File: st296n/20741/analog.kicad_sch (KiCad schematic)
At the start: 189 parts, among them J3 POWER, J4 SPINDLE, J5 STEPPER, J6 HEADS, Q1 ?, Q10 ?, Q11 ?, Q12 ?, Q15 "1A", Q2 2SD1760, Q3 IRFD110, Q4 IRFD110, Q5 IRFD110, Q8 ?, Q9 ?, U27 74LS00, U3 74LS14, U8 11747-501

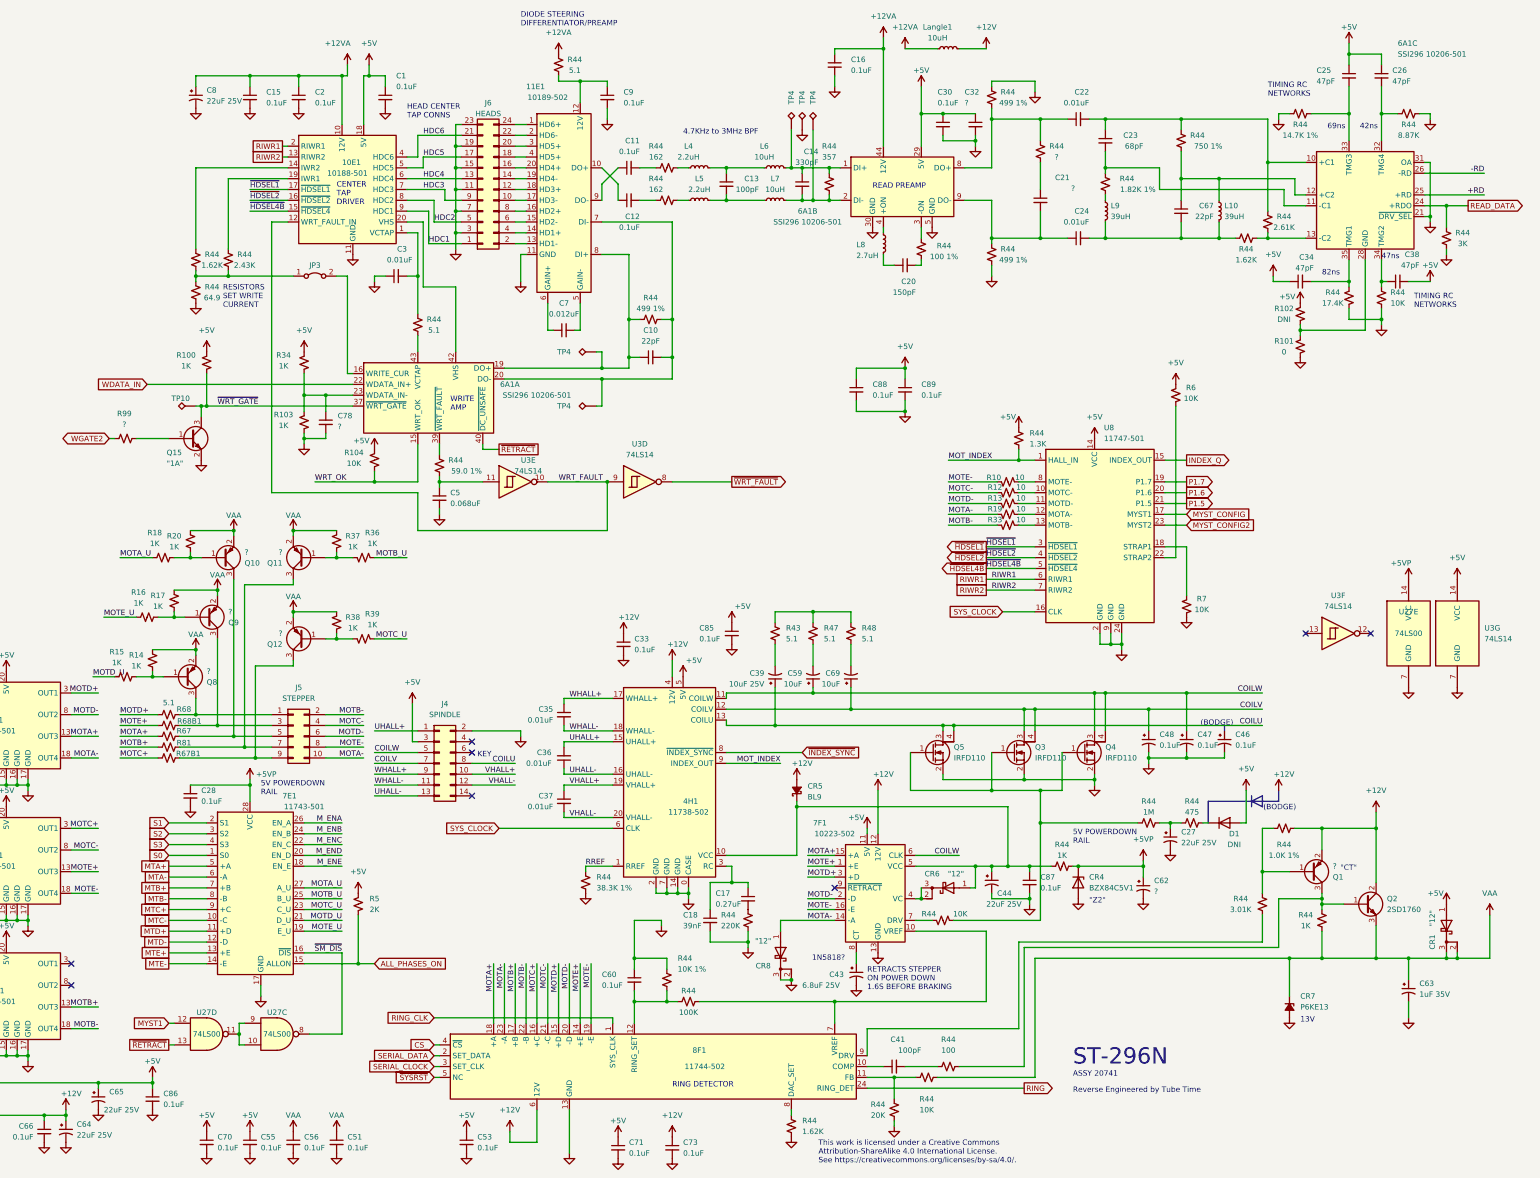
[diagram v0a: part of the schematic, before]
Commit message: st296n fix passives
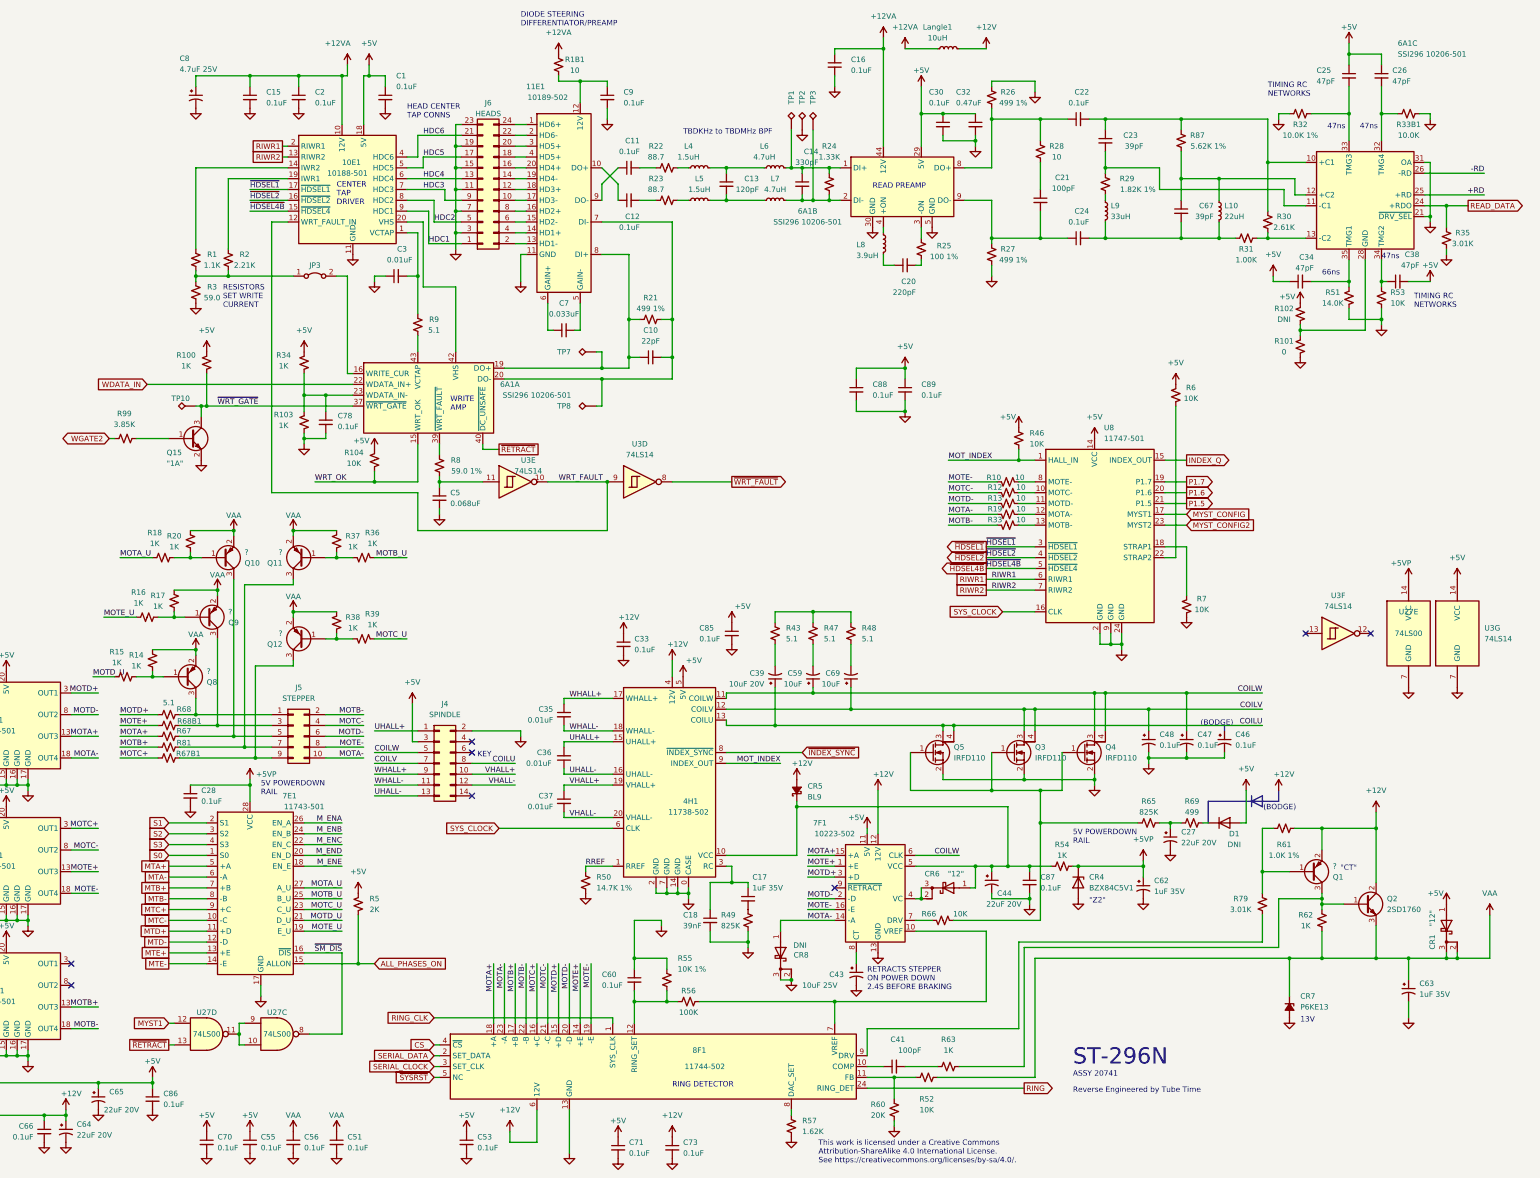
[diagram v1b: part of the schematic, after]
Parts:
- C13: value 100pF -> 120pF
- C17: value 0.27uF -> 1uF 35V
- C20: value 150pF -> 220pF
- C21: value ? -> 100pF
- C22, C24: value 0.01uF -> 0.1uF
- C23: value 68pF -> 39pF
- C27, C44, C64, C65: value 22uF 25V -> 22uF 20V
- C32: value ? -> 0.47uF
- C39: value 10uF 25V -> 10uF 20V
- C43: value 6.8uF 25V -> 10uF 25V
- C62: value ? -> 1uF 35V
- C67: value 22pF -> 39pF
- C7: value 0.012uF -> 0.033uF
- C78: value ? -> 0.1uF
- C8: value 22uF 25V -> 4.7uF 25V
- CR8: value "12" -> DNI
- L10: value 39uH -> 22uH
- L4, L5: value 2.2uH -> 1.5uH
- L6, L7: value 10uH -> 4.7uH
- L8: value 2.7uH -> 3.9uH
- L9: value 39uH -> 33uH
- R1: renamed from R44; value 1.62K -> 1.1K
- R1B1: renamed from R44; value 5.1 -> 10
- R2: renamed from R44; value 2.43K -> 2.21K
- R22, R23: renamed from R44; value 162 -> 88.7
- R24: renamed from R44; value 357 -> 1.33K
- R28: renamed from R44; value ? -> 10
- R3: renamed from R44; value 64.9 -> 59.0
- R31: renamed from R44; value 1.62K -> 1.00K
- R32: renamed from R44; value 14.7K 1% -> 10.0K 1%
- R33B1: renamed from R44; value 8.87K -> 10.0K
- R35: renamed from R44; value 3K -> 3.01K
- R46: renamed from R44; value 1.3K -> 10K
- R49: renamed from R44; value 220K -> 825K
- R50: renamed from R44; value 38.3K 1% -> 14.7K 1%
- R51: renamed from R44; value 17.4K -> 14.0K
- R63: renamed from R44; value 100 -> 1K
- R65: renamed from R44; value 1M -> 825K
- R69: renamed from R44; value 475 -> 499
- R87: renamed from R44; value 750 1% -> 5.62K 1%
- R99: value ? -> 3.85K
- renumbered R44 to R21, R44 to R25, R44 to R26, R44 to R27, R44 to R29, R44 to R30, R44 to R52, R44 to R53, R44 to R54, R44 to R55, R44 to R56, R44 to R57, R44 to R60, R44 to R61, R44 to R62, R44 to R66, R44 to R79, R44 to R8, R44 to R9, TP4 to TP1, TP4 to TP2, TP4 to TP3, TP4 to TP7, TP4 to TP8
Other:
- note added: "66ns"
- note added: "RETRACTS STEPPER ON POWER DOWN 2.4S BEFORE BRAKING"
- note added: "TBDKHz to TBDMHz BPF"
- note removed: "1N5818?"
- note removed: "4.7KHz to 3MHz BPF"
- note removed: "42ns"
- note removed: "69ns"
- note removed: "82ns"
- note removed: "RETRACTS STEPPER ON POWER DOWN 1.6S BEFORE BRAKING"

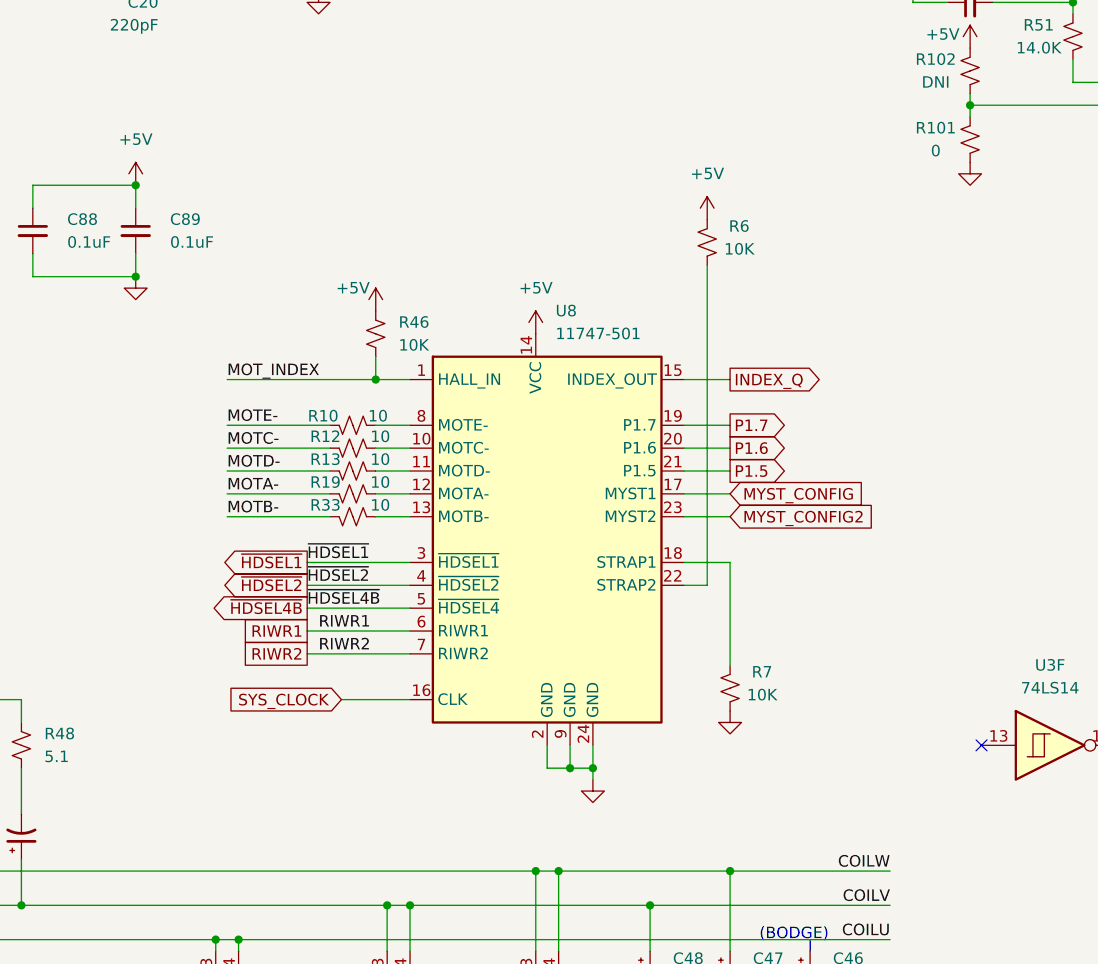
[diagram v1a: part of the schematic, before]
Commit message: st296n update symbol with more chip info
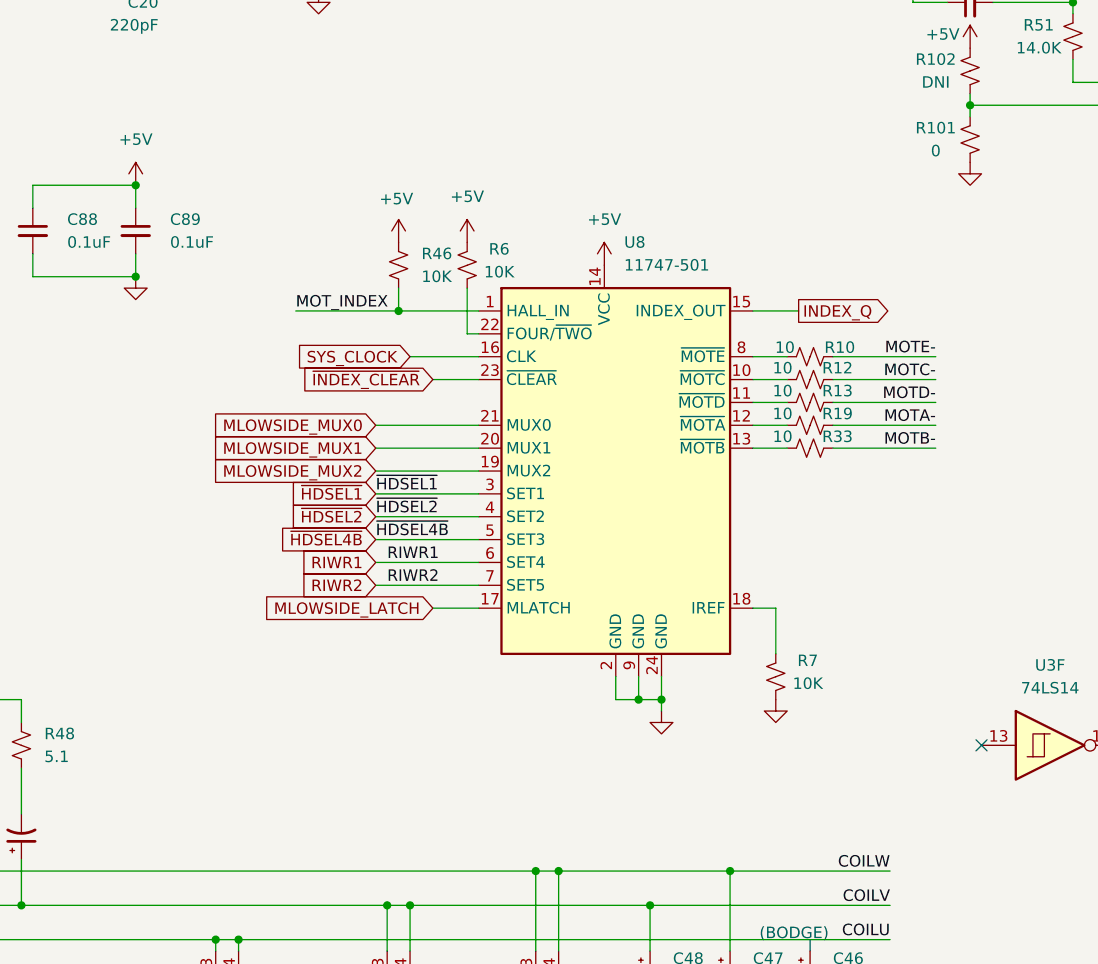
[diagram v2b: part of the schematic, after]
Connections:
- net MYST_CONFIG renamed MLOWSIDE_LATCH
- net MYST_CONFIG2 renamed ~{INDEX_CLEAR}
- net P1.5 renamed MLOWSIDE_MUX0
- net P1.6 renamed MLOWSIDE_MUX1
- net P1.7 renamed MLOWSIDE_MUX2
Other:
- moved on the sheet: R10, R12, R13, R19, R33, R46, R6, R7, U8
